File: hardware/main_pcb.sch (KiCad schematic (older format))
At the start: 80 parts

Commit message: MCU UPDATE
added MCU
added fuelgauge
removed unnessessary stuff
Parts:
- removed IC?: LM3914N, DIL18, symbol LM3914N
- added C? (x4): 100nF, symbol C_Small
- added C?: 104pF, symbol C_Small
- added R? (x2): 5k, symbol R_Small
- added U?: ATMEGA328P-AU, Housings_QFP:TQFP-32_7x7mm_Pitch0.8mm, symbol ATMEGA328P-AU
- added U?: MAX17043, MODULE, symbol MAX17043
- added Y?: 8MHz, symbol Crystal_Small
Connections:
- net BAT+: now also C?.1, R?.1, R?.1, U?.2 (CELL), U?.4 (VCC), U?.6 (VCC)
- net GND: now also C?.1, C?.2, C?.2, C?.2, U?.1 (CTG), U?.21 (GND), U?.3 (GND), U?.4 (GND), U?.5 (GND), U?.6 (QSTRT)
- net FAULT: now reaches U?.10 (FAULT)
- new net: C?.2, U?.20 (AREF)
- new net: C?.1, U?.7 ((PCINT6/XTAL1/TOSC1)PB6), Y?.2
- new net: C?.2, U?.8 ((PCINT7/XTAL2/TOSC2)PB7), Y?.1
- new net MAX_VCC: C?.1, U?.3 (VDD)
- new net MISO: U?.16 ((PCINT4/MISO)PB4)
- new net MOSI: U?.15 ((PCINT3/OC2A/MOSI)PB3)
- new net RX: U?.30 ((PCINT16/RXD)PD0)
- new net SCK: U?.17 ((PCINT5/SCK)PB5)
- new net SCL: R?.2, U?.28 ((PCINT13/SCL/ADC5)PC5), U?.7 (SCL)
- new net SDA: R?.2, U?.27 ((PCINT12/SDA/ADC4)PC4), U?.8 (SDA)
- new net TX: U?.31 ((PCINT17/TXD)PD1)
- new net battest_int: U?.32 ((PCINT18/INT0)PD2)
- new net onoff_int: U?.1 ((PCINT19/OC2B/INT1)PD3)
- new net ~ALRT: U?.5 (~ALRT)
- new net ~RESET: U?.29 ((PCINT14/~RESET~)PC6)
- no-connect marks 6 -> 5
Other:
- note added: "RTC over I2C\nfor RPi"
- note added: "adc not needed"
- note added: "hardware interrupts"
- note added: "levelshifter?\nuart_bat+ <-> uart_3V3"
- moved on the sheet: D?, R?, SW?

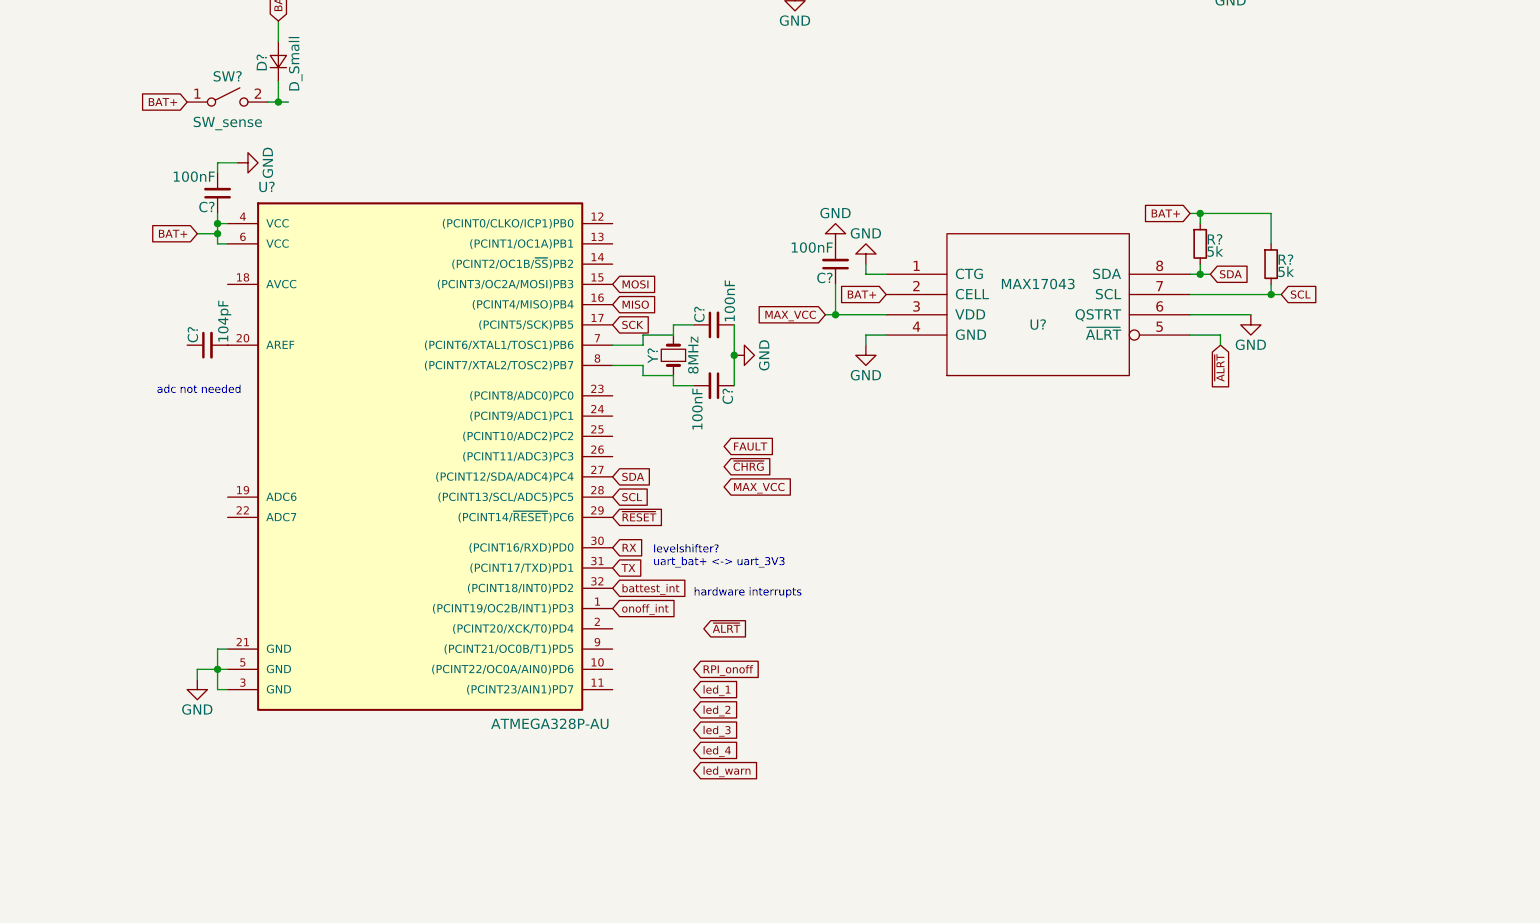
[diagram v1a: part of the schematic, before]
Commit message: added ISP connector
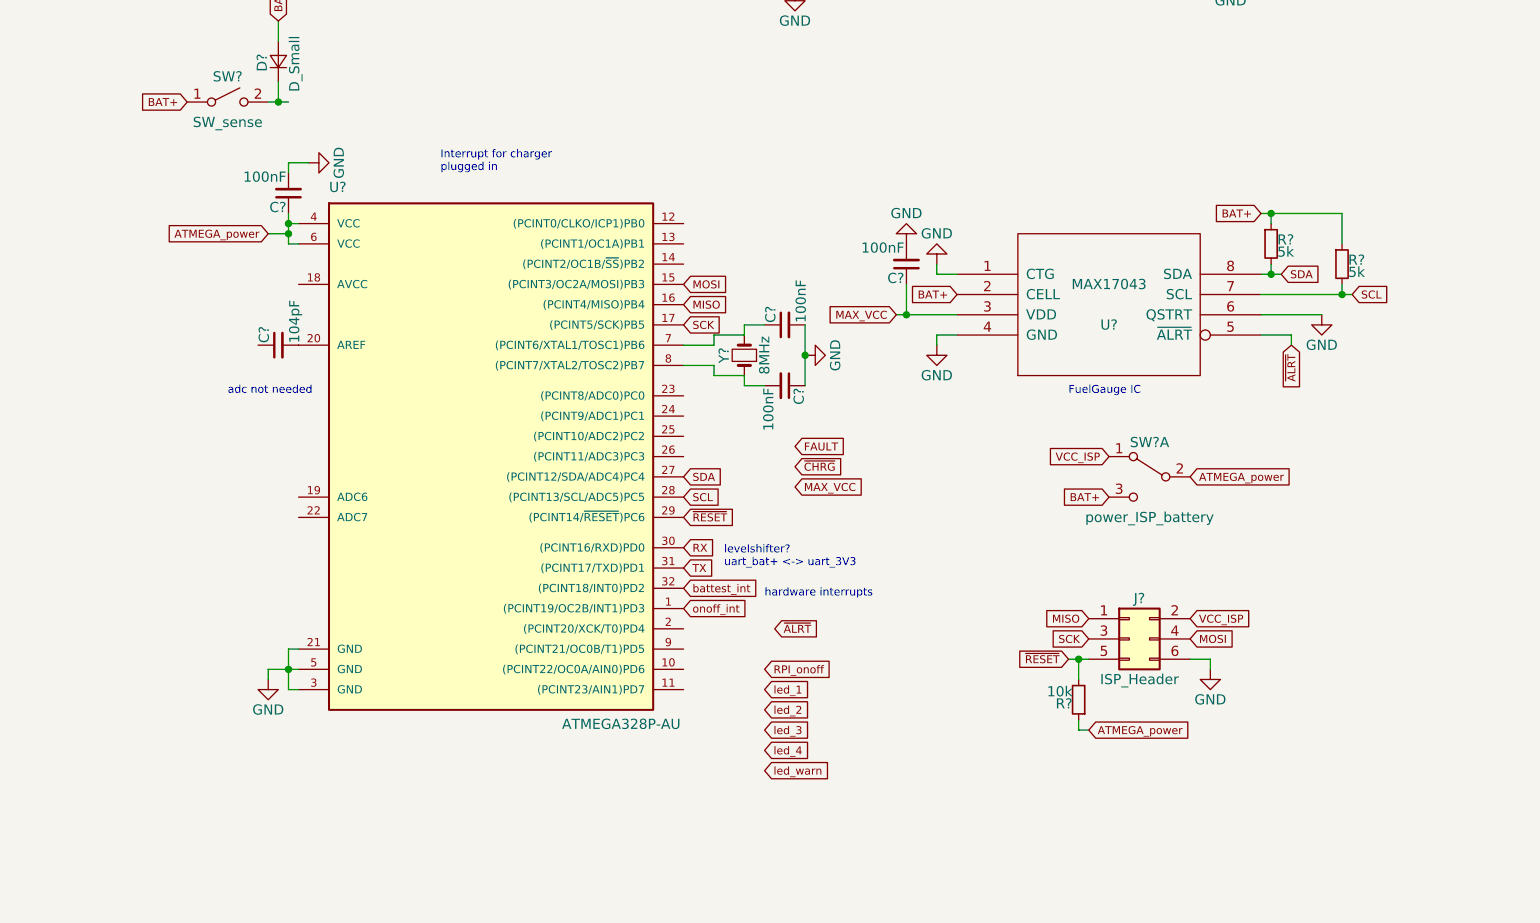
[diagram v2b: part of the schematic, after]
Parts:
- added J?: ISP_Header, symbol Conn_02x03_Odd_Even
- added R?: 10k, symbol R_Small
- added SW?: power_ISP_battery, symbol SW_DPDT_x2
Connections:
- net BAT+: now also SW?.3 (C); no longer C?.1, U?.4 (VCC), U?.6 (VCC)
- net GND: now also J?.6 (Pin_6)
- net MISO: now also J?.1 (Pin_1)
- net MOSI: now also J?.4 (Pin_4)
- net SCK: now also J?.3 (Pin_3)
- net ~RESET: now also J?.5 (Pin_5), R?.2
- new net ATMEGA_power: C?.1, R?.1, SW?.2 (B), U?.4 (VCC), U?.6 (VCC)
- new net VCC_ISP: J?.2 (Pin_2), SW?.1 (A)
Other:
- note added: "FuelGauge IC"
- note added: "Interrupt for charger\nplugged in"
- moved on the sheet: C?, R?, U?, Y?
